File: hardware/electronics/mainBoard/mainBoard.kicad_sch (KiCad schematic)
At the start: 0 parts

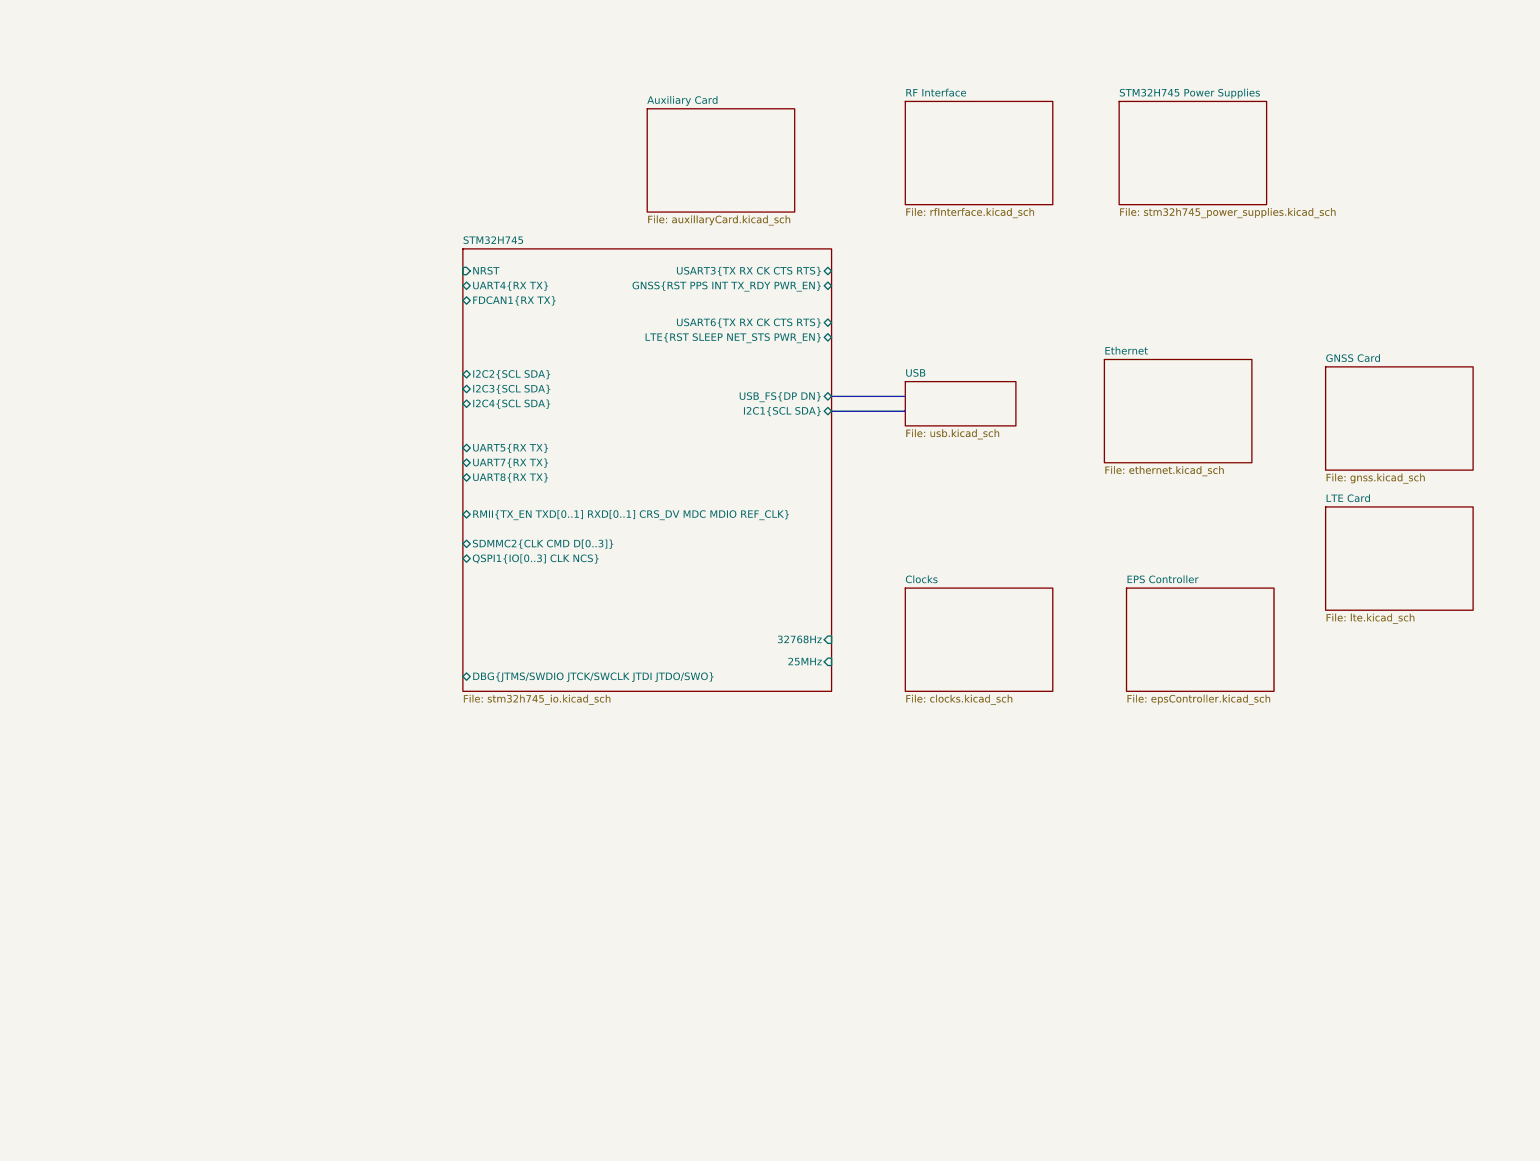
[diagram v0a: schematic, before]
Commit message: added GPIO for AUX card, EPS controller
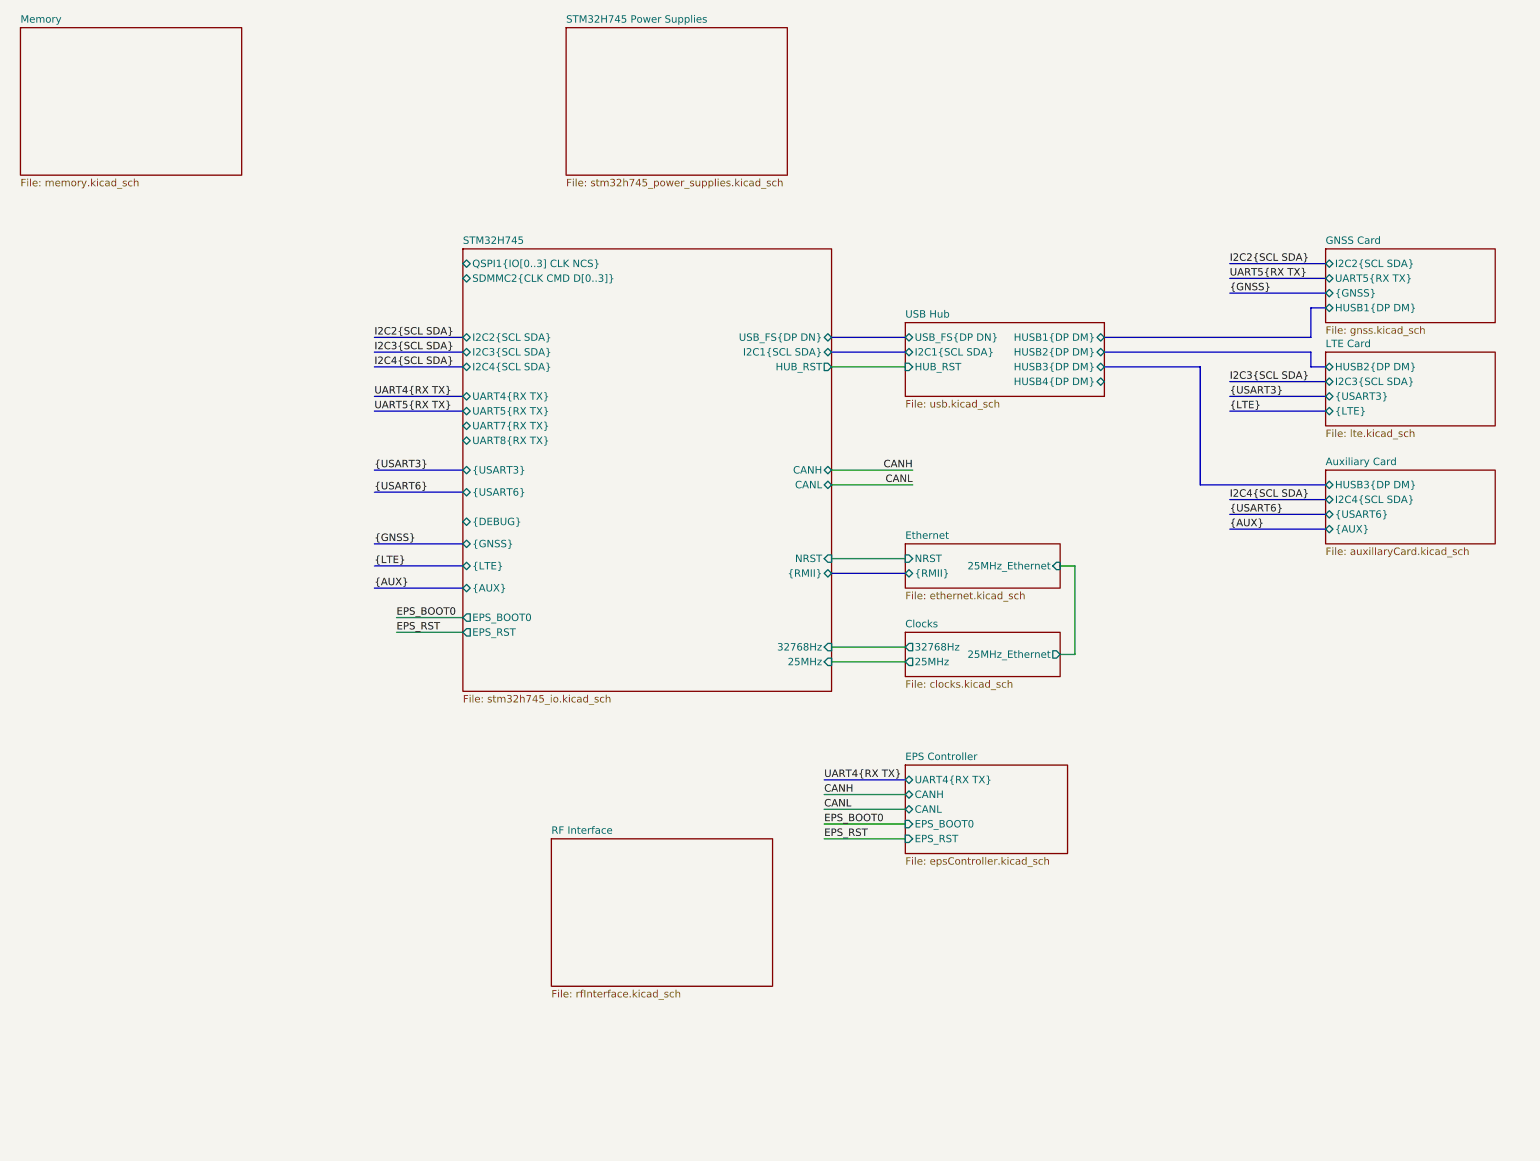
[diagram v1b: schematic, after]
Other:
- sheet USB renamed USB Hub
- added sheet Memory (memory.kicad_sch)
- sheet Auxiliary Card ports: added HUSB3{DP DM}, I2C4{SCL SDA}, {AUX}, {USART6}; removed none
- sheet Clocks ports: added 25MHz, 25MHz_Ethernet, 32768Hz; removed none
- sheet EPS Controller ports: added CANH, CANL, EPS_BOOT0, EPS_RST, UART4{RX TX}; removed none
- sheet Ethernet ports: added 25MHz_Ethernet, NRST, {RMII}; removed none
- sheet GNSS Card ports: added HUSB1{DP DM}, I2C2{SCL SDA}, UART5{RX TX}, {GNSS}; removed none
- sheet LTE Card ports: added HUSB2{DP DM}, I2C3{SCL SDA}, {LTE}, {USART3}; removed none
- sheet STM32H745 ports: added CANH, CANL, EPS_BOOT0, EPS_RST, HUB_RST, {AUX}, {DEBUG}, {GNSS}, {LTE}, {RMII}, {USART3}, {USART6}; removed DBG{JTMS/SWDIO JTCK/SWCLK JTDI JTDO/SWO}, FDCAN1{RX TX}, GNSS{RST PPS INT TX_RDY PWR_EN}, LTE{RST SLEEP NET_STS PWR_EN}, RMII{TX_EN TXD[0..1] RXD[0..1] CRS_DV MDC MDIO REF_CLK}, USART3{TX RX CK CTS RTS}, USART6{TX RX CK CTS RTS}
- sheet USB Hub ports: added HUB_RST, HUSB1{DP DM}, HUSB2{DP DM}, HUSB3{DP DM}, HUSB4{DP DM}, I2C1{SCL SDA}, USB_FS{DP DN}; removed none

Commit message: added nets to sheets
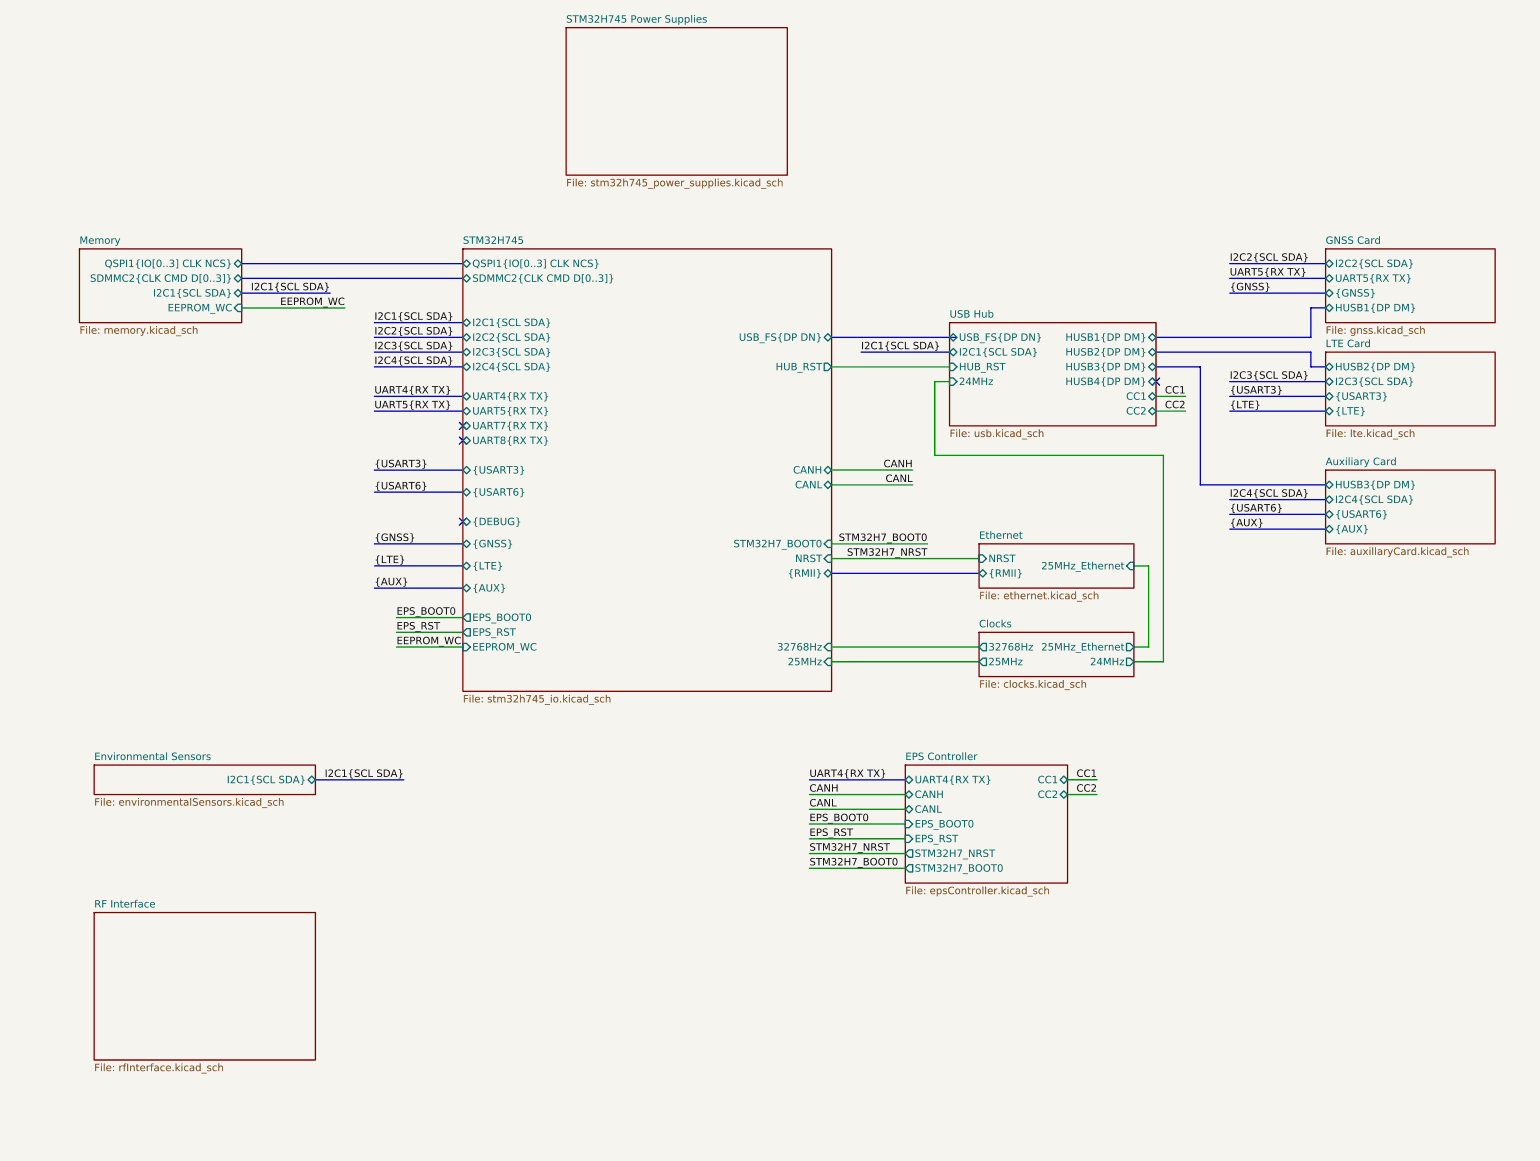
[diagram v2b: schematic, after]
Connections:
- no-connect marks 0 -> 4
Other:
- added sheet Environmental Sensors (environmentalSensors.kicad_sch)
- sheet Clocks ports: added 24MHz; removed none
- sheet EPS Controller ports: added CC1, CC2, STM32H7_BOOT0, STM32H7_NRST; removed none
- sheet Memory ports: added EEPROM_WC, I2C1{SCL SDA}, QSPI1{IO[0..3] CLK NCS}, SDMMC2{CLK CMD D[0..3]}; removed none
- sheet STM32H745 ports: added EEPROM_WC, STM32H7_BOOT0; removed none
- sheet USB Hub ports: added 24MHz, CC1, CC2; removed none

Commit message: reorganized sheet
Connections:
- no-connect marks 4 -> 0
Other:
- removed sheet STM32H745 Power Supplies
- removed sheet USB Hub
- sheet Auxiliary Card: file auxillaryCard.kicad_sch -> auxillary.kicad_sch
- sheet Auxiliary Card ports: added none; removed HUSB3{DP DM}
- sheet Clocks ports: added none; removed 24MHz
- sheet EPS Controller ports: added H7_BOOT0, H7_NRST, L0_BOOT0, L0_NRST, USB_FS{DP DN}; removed CC1, CC2, EPS_BOOT0, EPS_RST, STM32H7_BOOT0, STM32H7_NRST
- sheet Environmental Sensors: file environmentalSensors.kicad_sch -> sensors.kicad_sch
- sheet GNSS Card ports: added none; removed HUSB1{DP DM}
- sheet LTE Card ports: added none; removed HUSB2{DP DM}
- sheet STM32H745: file stm32h745_io.kicad_sch -> stm32h745.kicad_sch
- sheet STM32H745 ports: added H7_BOOT0, H7_NRST, L0_BOOT0, L0_NRST; removed EPS_BOOT0, EPS_RST, HUB_RST, NRST, STM32H7_BOOT0, UART7{RX TX}, UART8{RX TX}, {DEBUG}

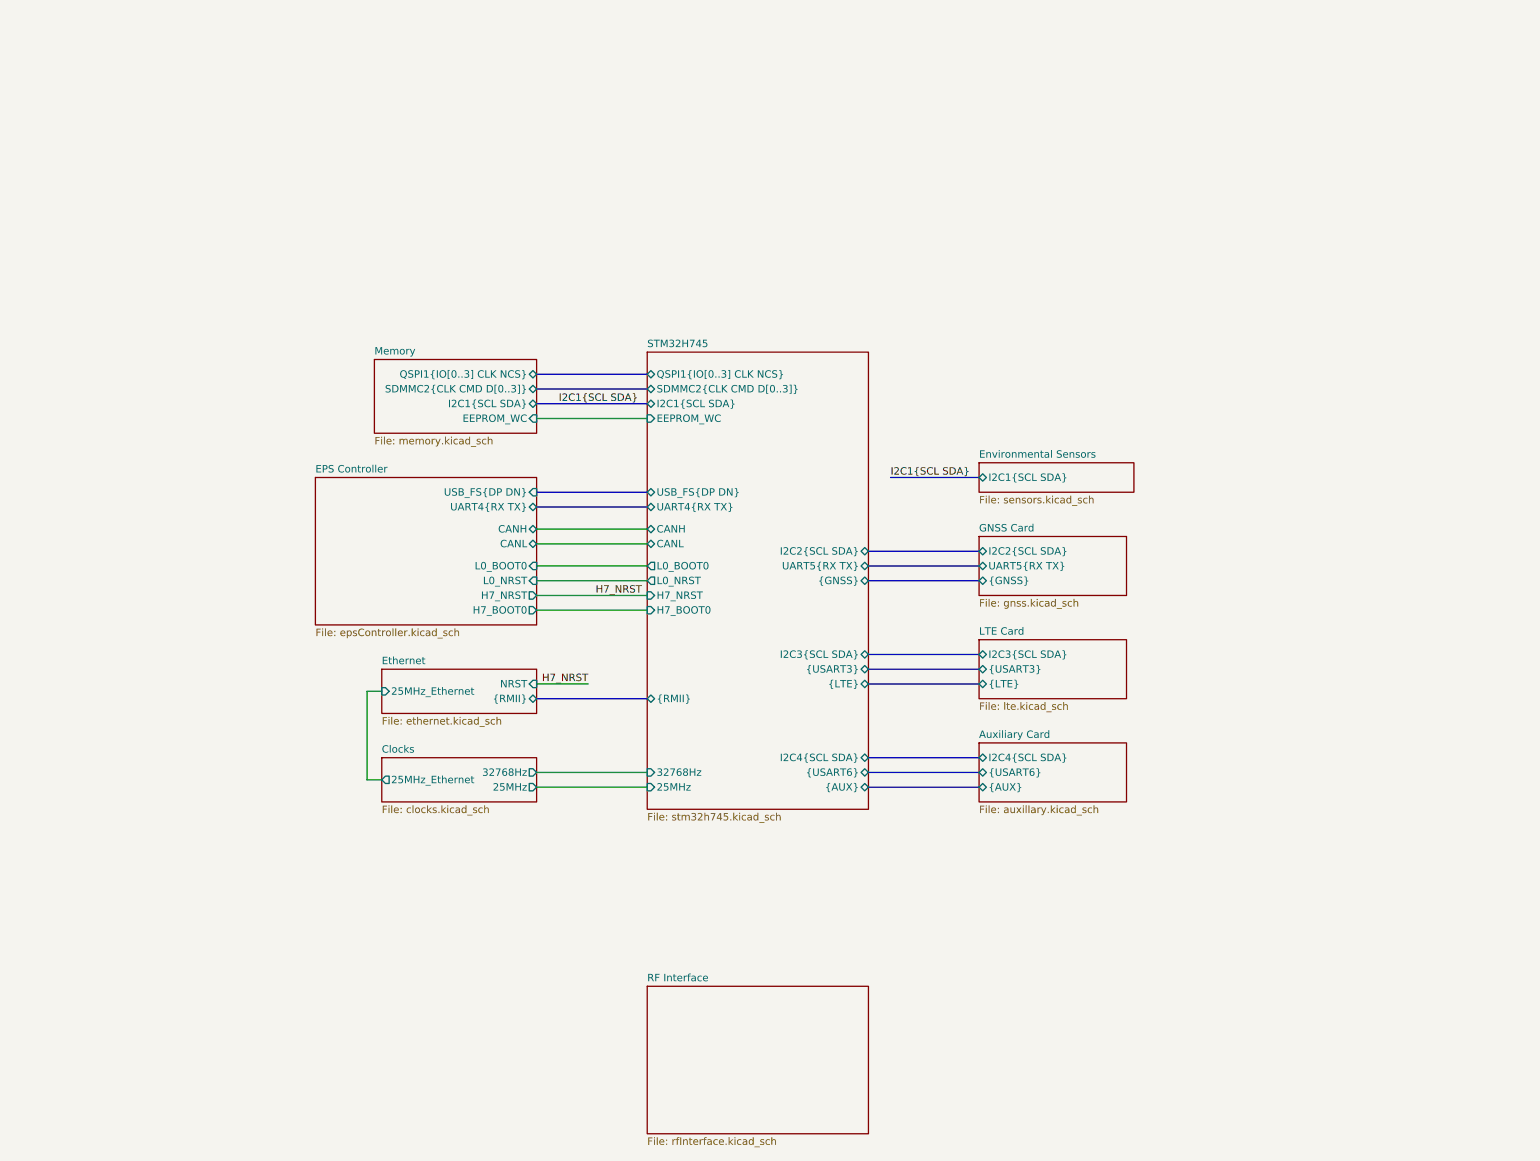
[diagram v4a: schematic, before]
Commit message: moved CAN transceivers to their own page
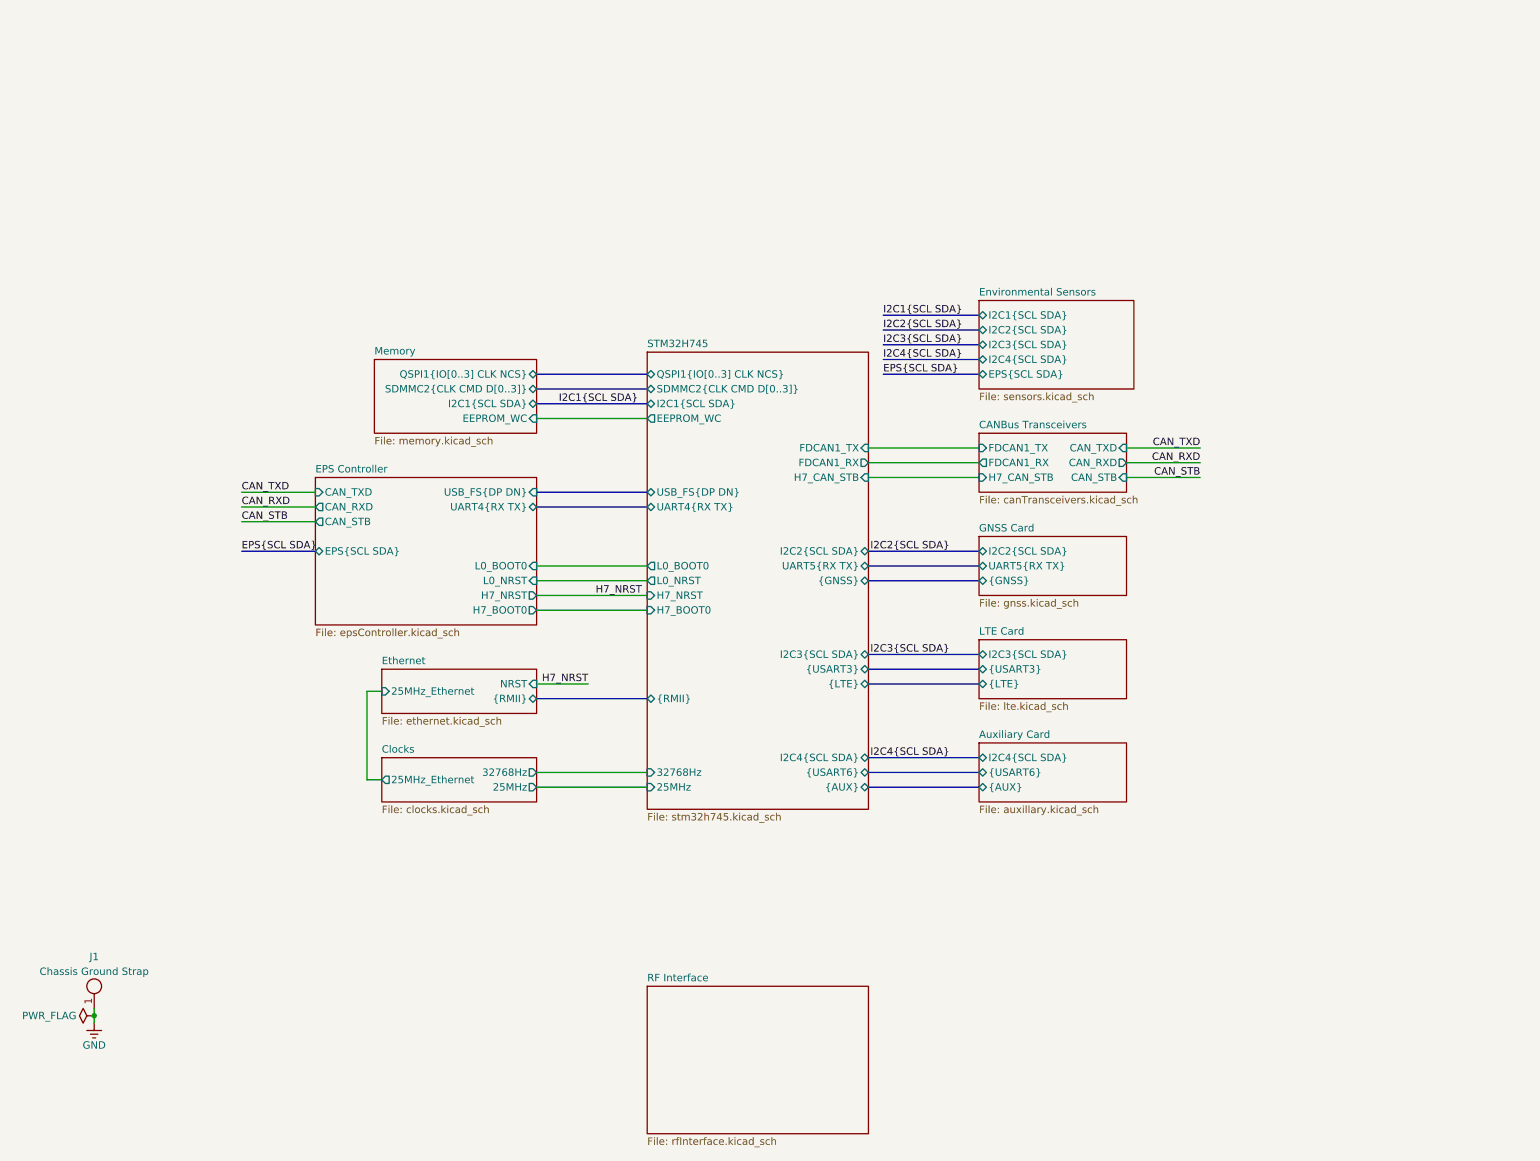
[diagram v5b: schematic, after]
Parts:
- added J1: Chassis Ground Strap, lib_connectors:M4.5-MH, symbol lib_sch:Mounting-Hole
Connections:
- new net GND: J1.1
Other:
- added sheet CANBus Transceivers (canTransceivers.kicad_sch)
- sheet EPS Controller ports: added CAN_RXD, CAN_STB, CAN_TXD, EPS{SCL SDA}; removed CANH, CANL
- sheet Environmental Sensors ports: added EPS{SCL SDA}, I2C2{SCL SDA}, I2C3{SCL SDA}, I2C4{SCL SDA}; removed none
- sheet STM32H745 ports: added FDCAN1_RX, FDCAN1_TX, H7_CAN_STB; removed CANH, CANL

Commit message: assigned footprints
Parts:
- J1: footprint lib_connectors:M4.5-MH -> lib_misc:M4.5-MH
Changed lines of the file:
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@@
 	(title_block
 		(title "System Diagram")
-		(date "2025-03-15")
+		(date "2025-03-20")
 		(rev "1")
 		(comment 2 "PROTOTYPE")
@@
 			)
 		)
-		(property "Footprint" "lib_connectors:M4.5-MH"
+		(property "Footprint" "lib_misc:M4.5-MH"
 			(at 25.4 177.8 0)
 			(effects
